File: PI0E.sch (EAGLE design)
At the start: 38 parts, among them T1 WE-LAN-10/100/1000-BASE-T,749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, X1 22-23-2021, X2 22-23-2021

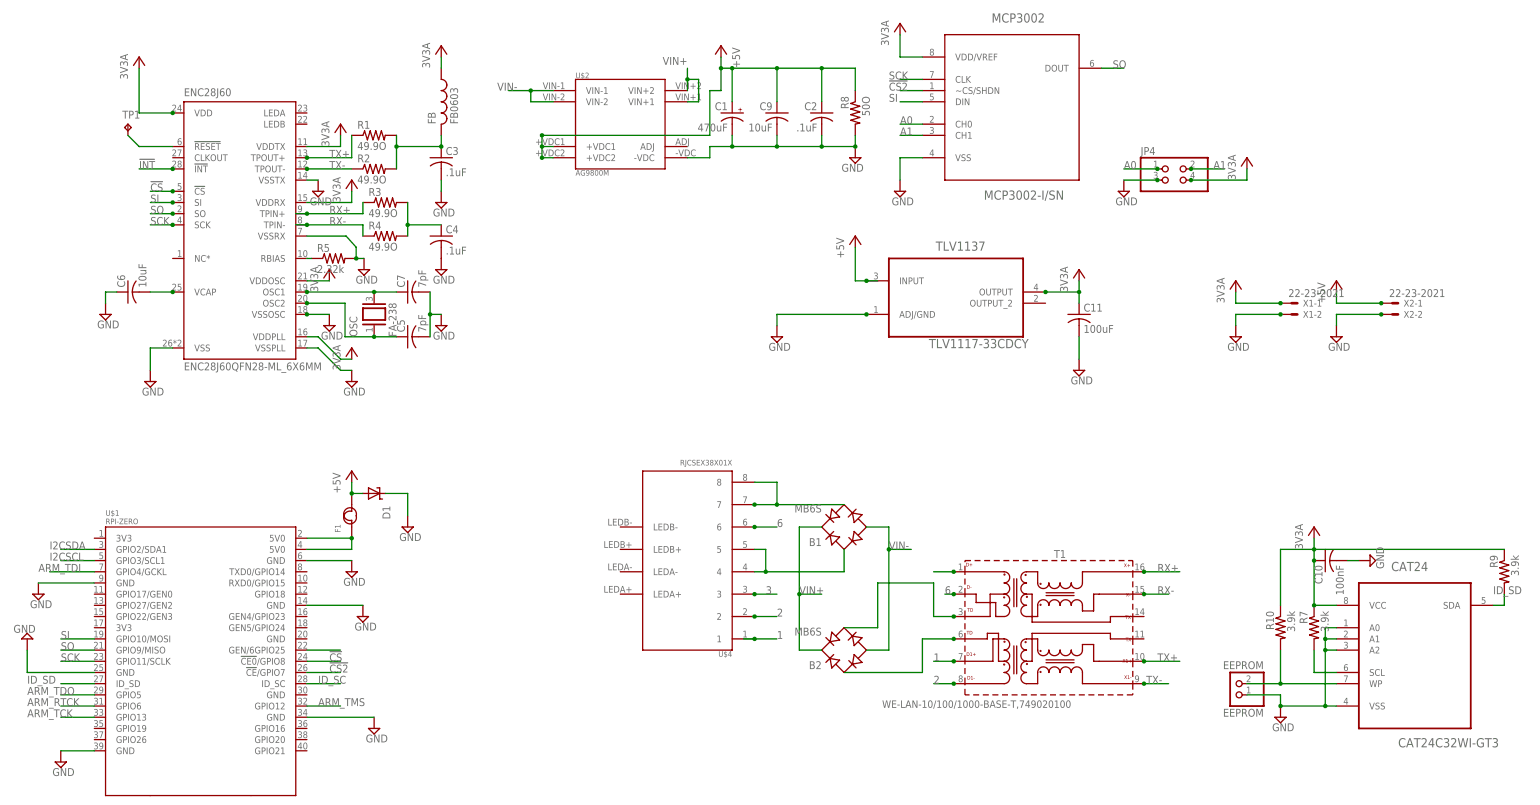
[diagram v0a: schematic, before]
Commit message: Changed layout to match RPi 0 form factor more closely
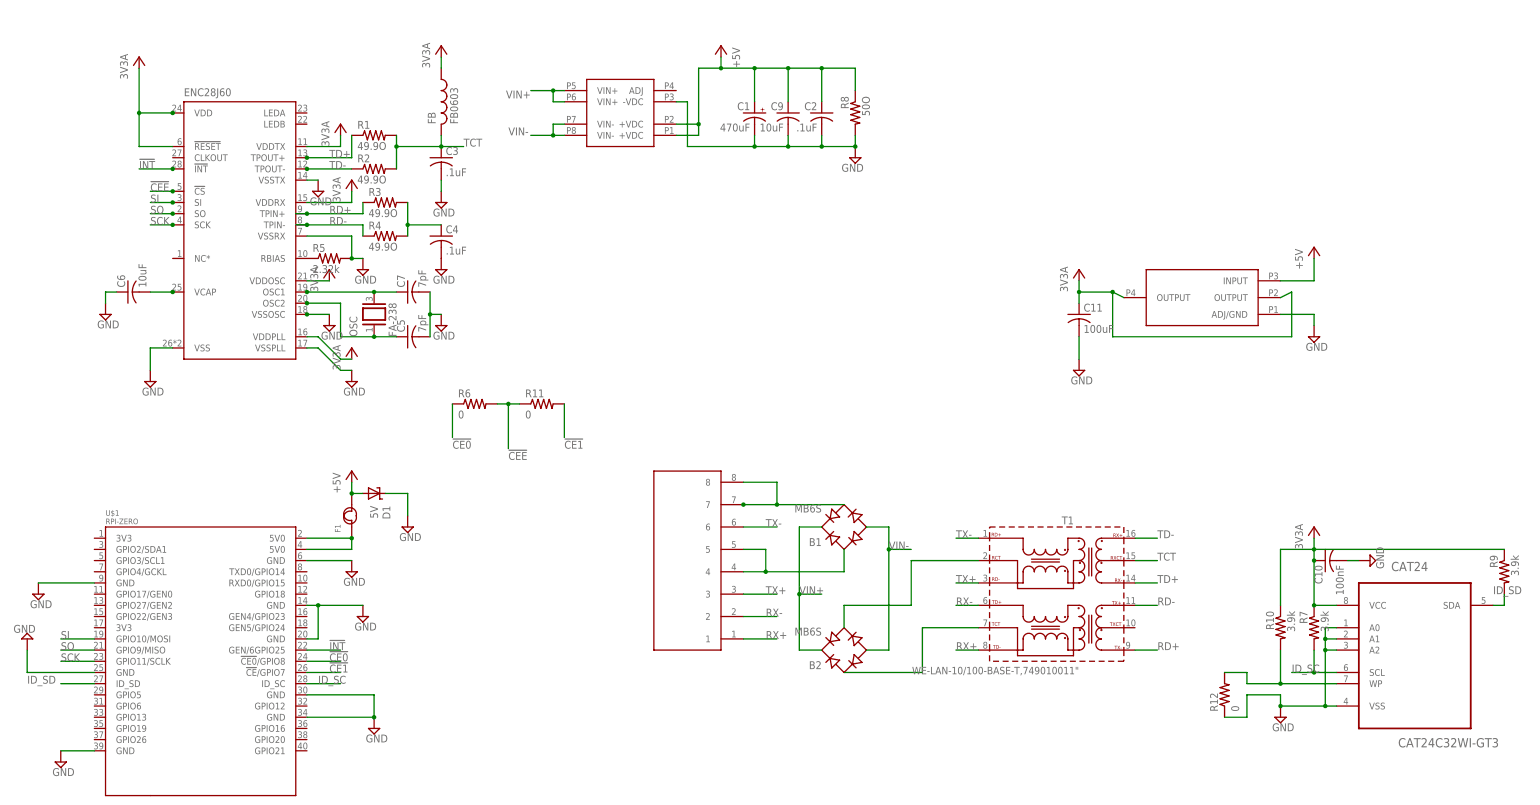
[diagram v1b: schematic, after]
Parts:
- removed EEPROM: EEPROM, pinhead:PINHD-1X2
- removed JP4: (no value), pinhead:PINHD-2X2
- removed MCP3002: MCP3002-I/SN, Microchip_By_element14_Batch_1:MCP3002-I/SN
- removed TLV1137: TLV1117-33CDCY, Texas Instruments_By_element14_Batch_1:TLV1117-33CDCY
- removed TP1: TPB1,27, testpad:TPB1,27
- removed X1, X2: 22-23-2021, con-molex:22-23-2021
- added R11, R12, R6: 0, resistor:R-US_R0603
- added U$3: TLV1117TLV1117DCY, texas_instruments:TLV1117TLV1117DCY
- D1: value (none) -> 5V
- T1: value WE-LAN-10/100/1000-BASE-T,749020100 -> WE-LAN-10/100-BASE-T,749010011"; device EagleLibrary_Wuerth_Elektronik_eiSos_V4_20130318:WE-LAN-10/100/1000-BASE-T,749020100 -> EagleLibrary_Wuerth_Elektronik_eiSos_rev16a:WE-LAN-10/100-BASE-T,749010011"
- U$2: value AG9800M -> AG9800AG9800M; device ENC28J60-QFN:AG9800M -> silvertell:AG9800AG9800M
- U$4: value RJCSEX38X01X -> RJCSEX38X01XRJCSEX38X01X; device ENC28J60-QFN:RJCSEX38X01X -> rj45:RJCSEX38X01XRJCSEX38X01X
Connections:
- removed net !CS: ENC28J60.!CS, U$1.!CE0!/GPIO8
- removed net !CS2: MCP3002.~CS/SHDN, U$1.!CE!/GPIO7
- removed net 1: T1.D1+, U$4.1
- removed net 2: T1.D1-, U$4.2
- removed net 3: T1.D+, U$4.3
- removed net 6: T1.D-, U$4.6
- removed net A0: JP4.1, MCP3002.CH0
- removed net A1: JP4.2, MCP3002.CH1
- removed net ARM_RTCK: U$1.GPIO6
- removed net ARM_TCK: U$1.GPIO13
- removed net ARM_TDI: U$1.GPIO4/GCKL
- removed net ARM_TDO: U$1.GPIO5
- removed net ARM_TMS: U$1.GPIO12
- removed net I2CSCL: U$1.GPIO3/SCL1
- removed net I2CSDA: U$1.GPIO2/SDA1
- removed net N$13: C3.1, FB.2, R1.2, R2.2
- removed net N$40: ENC28J60.!RESET, TP1.TP
- removed net N$9: B2.AC1, T1.TD2
- new net !CE0: R6.1, U$1.!CE0!/GPIO8
- new net !CE1: R11.2, U$1.!CE!/GPIO7
- new net !CEE: ENC28J60.!CS, R11.1, R6.2
- new net N$1: B2.AC1, T1G$1.TCT
- new net RD+: ENC28J60.TPIN+, R3.1, T1G$1.TX-
- new net RD-: ENC28J60.TPIN-, R4.1, T1G$1.TX+
- new net TCT: C3.1, FB.2, R1.2, R2.2, T1G$1.RXCT
- new net TD+: ENC28J60.TPOUT+, R1.1, T1G$1.RX-
- new net TD-: ENC28J60.TPOUT-, R2.1, T1G$1.RX+
- net +3V3: now also ENC28J60.!RESET, U$3.OUTPUT@1, U$3.OUTPUT@2; no longer JP4.4, MCP3002.VDD/VREF, TLV1137.OUTPUT, X1-1.S
- net +5V: now also U$2.+VDC@1, U$2.+VDC@2, U$3.INPUT; no longer TLV1137.INPUT, U$2.+VDC1, U$2.+VDC2, X2-1.S
- net GND: now also R12.1, U$1.GND@5, U$1.GND@6, U$3.ADJ/GND; no longer EEPROM.1, JP4.3, MCP3002.VSS, TLV1137.ADJ/GND, X1-2.S, X2-2.S
- net N$4: now also R12.2; no longer EEPROM.2
- net N$7: now also T1G$1.RCT; no longer T1.TD1
- net RX+: now also T1G$1.TD-, U$4.1; no longer ENC28J60.TPIN+, R3.1, T1.X+
- net RX-: now also T1G$1.TD+, U$4.2; no longer ENC28J60.TPIN-, R4.1, T1.X-
- net SCK: no longer MCP3002.CLK
- net SI: no longer MCP3002.DIN
- net SO: no longer MCP3002.DOUT
- net TX+: now also T1G$1.RD-, U$4.3; no longer ENC28J60.TPOUT+, R1.1, T1.X1+
- net TX-: now also T1G$1.RD+, U$4.6; no longer ENC28J60.TPOUT-, R2.1, T1.X1-
- net VIN+: now also U$2.VIN+@1, U$2.VIN+@2; no longer U$2.VIN+1, U$2.VIN+2
- net VIN-: now also U$2.VIN-@1, U$2.VIN-@2; no longer U$2.VIN-1, U$2.VIN-2
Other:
- moved on the sheet: C1, C9, R5

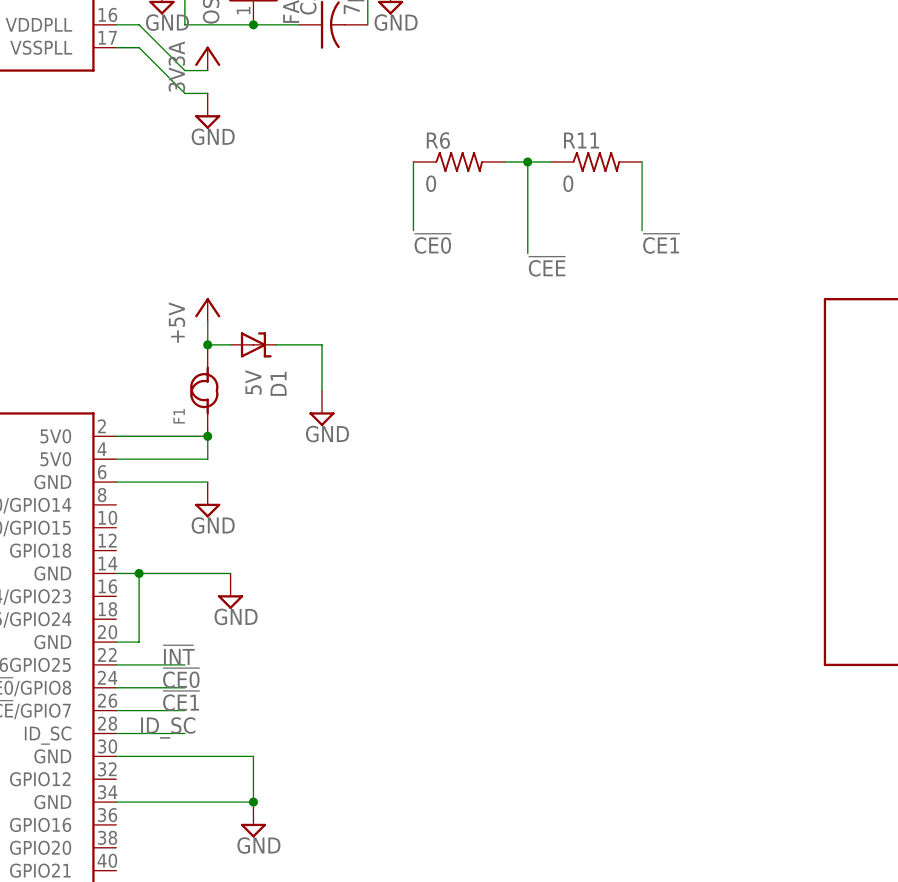
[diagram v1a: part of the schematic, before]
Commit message: Fixed silkscreen layer
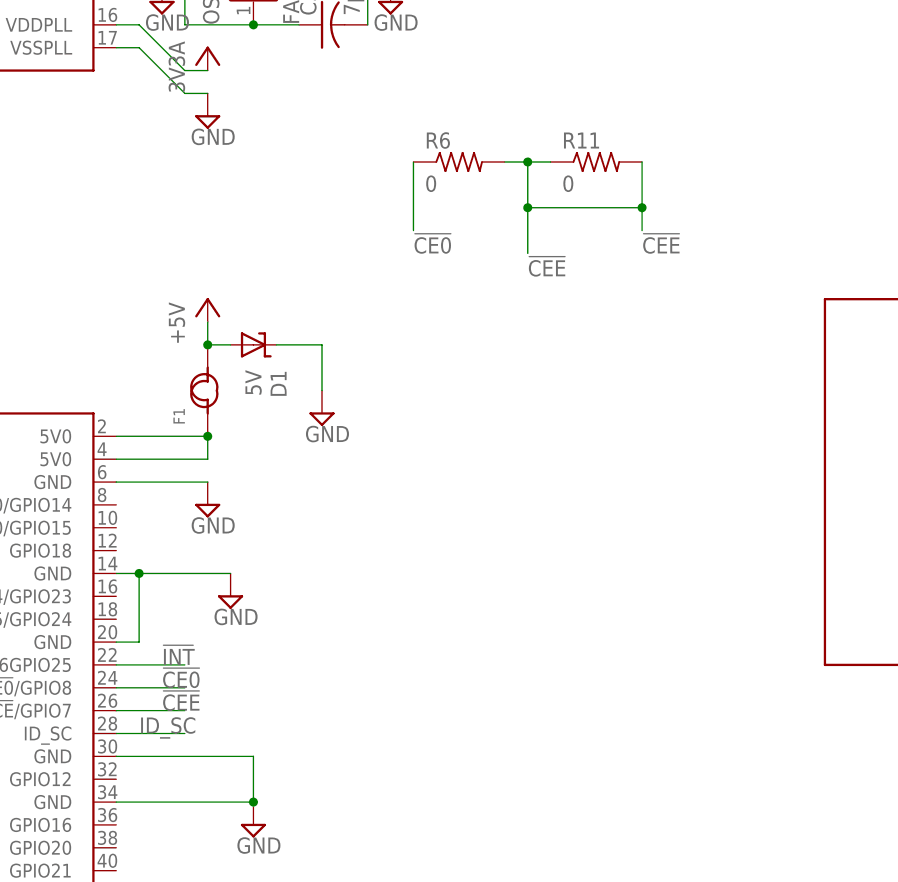
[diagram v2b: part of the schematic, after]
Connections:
- removed net !CE1: R11.2, U$1.!CE!/GPIO7
- net !CEE: now also R11.2, U$1.!CE!/GPIO7
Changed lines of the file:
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@@
-</segment>
-</net>
-<net name="!CE1" class="0">
-<segment>
-<pinref part="U$1" gate="G$1" pin="!CE!/GPIO7"/>
-<wire x1="73.66" y1="48.26" x2="81.28" y2="48.26" width="0.1524" layer="91"/>
-<label x="78.74" y="48.26" size="1.778" layer="95"/>
-</segment>
-<segment>
-<wire x1="132.08" y1="109.22" x2="132.08" y2="101.6" width="0.1524" layer="91"/>
-<label x="132.08" y="99.06" size="1.778" layer="95"/>
-<pinref part="R11" gate="G$1" pin="2"/>
 </segment>
 </net>
@@
 </segment>
 <segment>
-<wire x1="119.38" y1="109.22" x2="119.38" y2="99.06" width="0.1524" layer="91"/>
+<wire x1="119.38" y1="109.22" x2="119.38" y2="104.14" width="0.1524" layer="91"/>
 <label x="119.38" y="96.52" size="1.778" layer="95"/>
 <pinref part="R6" gate="G$1" pin="2"/>
+<wire x1="119.38" y1="104.14" x2="119.38" y2="99.06" width="0.1524" layer="91"/>
 <wire x1="116.84" y1="109.22" x2="119.38" y2="109.22" width="0.1524" layer="91"/>
 <pinref part="R11" gate="G$1" pin="1"/>
 <wire x1="119.38" y1="109.22" x2="121.92" y2="109.22" width="0.1524" layer="91"/>
 <junction x="119.38" y="109.22"/>
+<wire x1="132.08" y1="109.22" x2="132.08" y2="104.14" width="0.1524" layer="91"/>
+<label x="132.08" y="99.06" size="1.778" layer="95"/>
+<pinref part="R11" gate="G$1" pin="2"/>
+<wire x1="132.08" y1="104.14" x2="132.08" y2="101.6" width="0.1524" layer="91"/>
+<wire x1="119.38" y1="104.14" x2="132.08" y2="104.14" width="0.1524" layer="91"/>
+<junction x="119.38" y="104.14"/>
+<junction x="132.08" y="104.14"/>
+</segment>
+<segment>
+<pinref part="U$1" gate="G$1" pin="!CE!/GPIO7"/>
+<wire x1="73.66" y1="48.26" x2="81.28" y2="48.26" width="0.1524" layer="91"/>
+<label x="78.74" y="48.26" size="1.778" layer="95"/>
 </segment>
 </net>

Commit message: Changed default CE trace to CE0
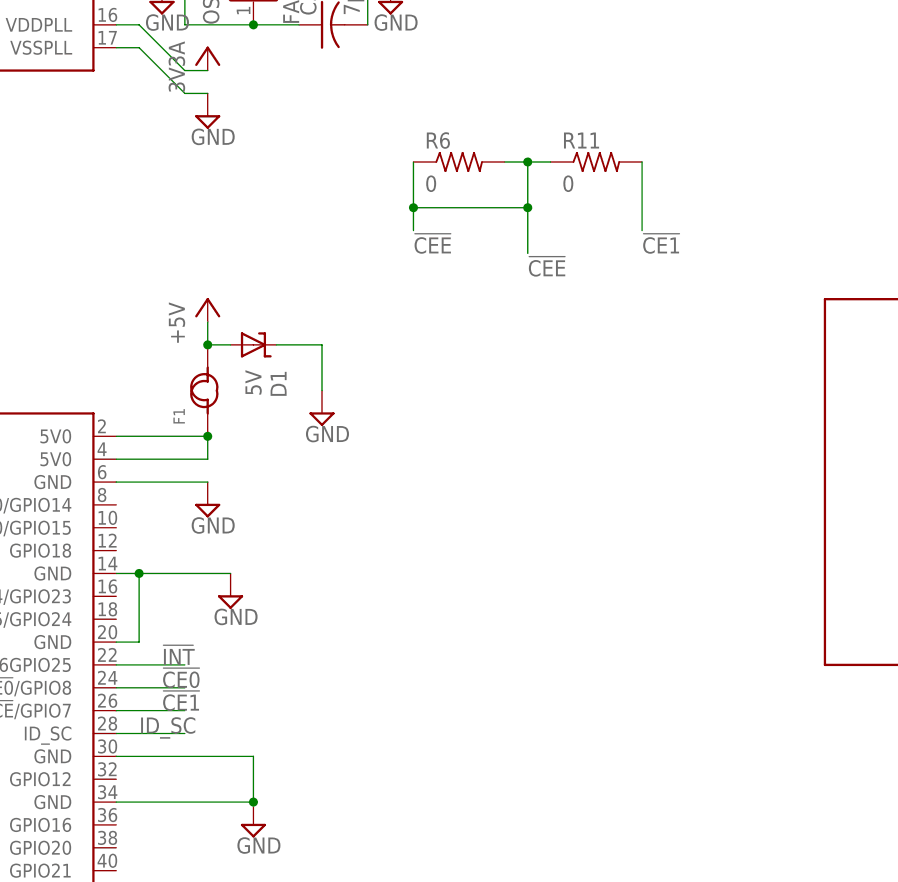
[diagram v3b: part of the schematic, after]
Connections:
- new net !CE1: R11.2, U$1.!CE!/GPIO7
- net !CE0: no longer R6.1
- net !CEE: now also R6.1; no longer R11.2, U$1.!CE!/GPIO7
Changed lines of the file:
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@@
 <label x="78.74" y="50.8" size="1.778" layer="95"/>
-</segment>
-<segment>
-<wire x1="106.68" y1="109.22" x2="106.68" y2="101.6" width="0.1524" layer="91"/>
-<label x="106.68" y="99.06" size="1.778" layer="95"/>
-<pinref part="R6" gate="G$1" pin="1"/>
 </segment>
 </net>
@@
 </segment>
 <segment>
-<wire x1="119.38" y1="109.22" x2="119.38" y2="104.14" width="0.1524" layer="91"/>
 <label x="119.38" y="96.52" size="1.778" layer="95"/>
 <pinref part="R6" gate="G$1" pin="2"/>
+<wire x1="119.38" y1="109.22" x2="119.38" y2="104.14" width="0.1524" layer="91"/>
 <wire x1="119.38" y1="104.14" x2="119.38" y2="99.06" width="0.1524" layer="91"/>
 <wire x1="116.84" y1="109.22" x2="119.38" y2="109.22" width="0.1524" layer="91"/>
@@
 <wire x1="119.38" y1="109.22" x2="121.92" y2="109.22" width="0.1524" layer="91"/>
 <junction x="119.38" y="109.22"/>
-<wire x1="132.08" y1="109.22" x2="132.08" y2="104.14" width="0.1524" layer="91"/>
-<label x="132.08" y="99.06" size="1.778" layer="95"/>
-<pinref part="R11" gate="G$1" pin="2"/>
-<wire x1="132.08" y1="104.14" x2="132.08" y2="101.6" width="0.1524" layer="91"/>
-<wire x1="119.38" y1="104.14" x2="132.08" y2="104.14" width="0.1524" layer="91"/>
+<pinref part="R6" gate="G$1" pin="1"/>
+<wire x1="106.68" y1="109.22" x2="106.68" y2="104.14" width="0.1524" layer="91"/>
+<label x="106.68" y="99.06" size="1.778" layer="95"/>
+<wire x1="106.68" y1="104.14" x2="106.68" y2="101.6" width="0.1524" layer="91"/>
+<wire x1="119.38" y1="104.14" x2="106.68" y2="104.14" width="0.1524" layer="91"/>
 <junction x="119.38" y="104.14"/>
-<junction x="132.08" y="104.14"/>
-</segment>
-<segment>
-<pinref part="U$1" gate="G$1" pin="!CE!/GPIO7"/>
-<wire x1="73.66" y1="48.26" x2="81.28" y2="48.26" width="0.1524" layer="91"/>
-<label x="78.74" y="48.26" size="1.778" layer="95"/>
+<junction x="106.68" y="104.14"/>
 </segment>
 </net>
@@
 </segment>
 </net>
+<net name="!CE1" class="0">
+<segment>
+<pinref part="R11" gate="G$1" pin="2"/>
+<wire x1="132.08" y1="109.22" x2="132.08" y2="101.6" width="0.1524" layer="91"/>
+<label x="132.08" y="99.06" size="1.778" layer="95"/>
+</segment>
+<segment>
+<pinref part="U$1" gate="G$1" pin="!CE!/GPIO7"/>
+<wire x1="73.66" y1="48.26" x2="81.28" y2="48.26" width="0.1524" layer="91"/>
+<label x="78.74" y="48.26" size="1.778" layer="95"/>
+</segment>
+</net>
